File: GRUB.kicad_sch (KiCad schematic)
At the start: 52 parts, among them J1 External controller, timer or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, J3 LEDs Drivers Connector, Q1 2N3904, Q2 2N3904, Q3 2N3904, Q5 2N3904, SW1 R_SWITCH, SW2 U_SWITCH, SW3 B_SWITCH, SW4 1) Focus 2) Safelight 3) Colo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

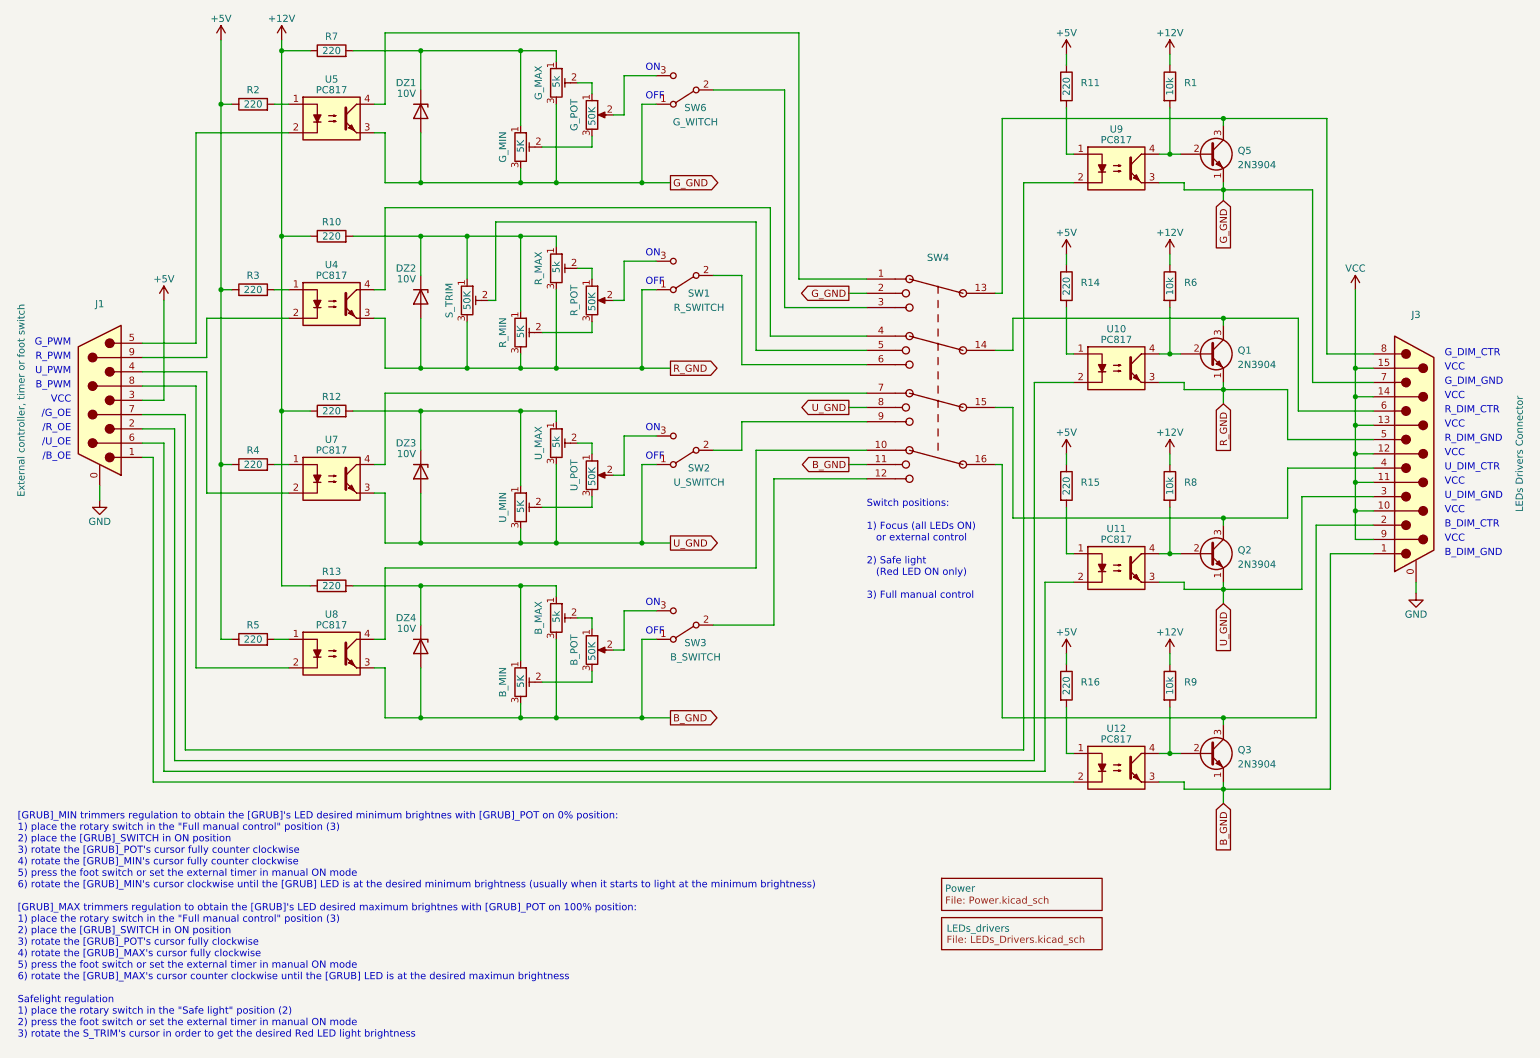
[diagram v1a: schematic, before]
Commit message: - Power rack alternatives: either two LM317s or LM7812 + LM7805 - Added channels SPDT selectors for foot switch or external output enable control
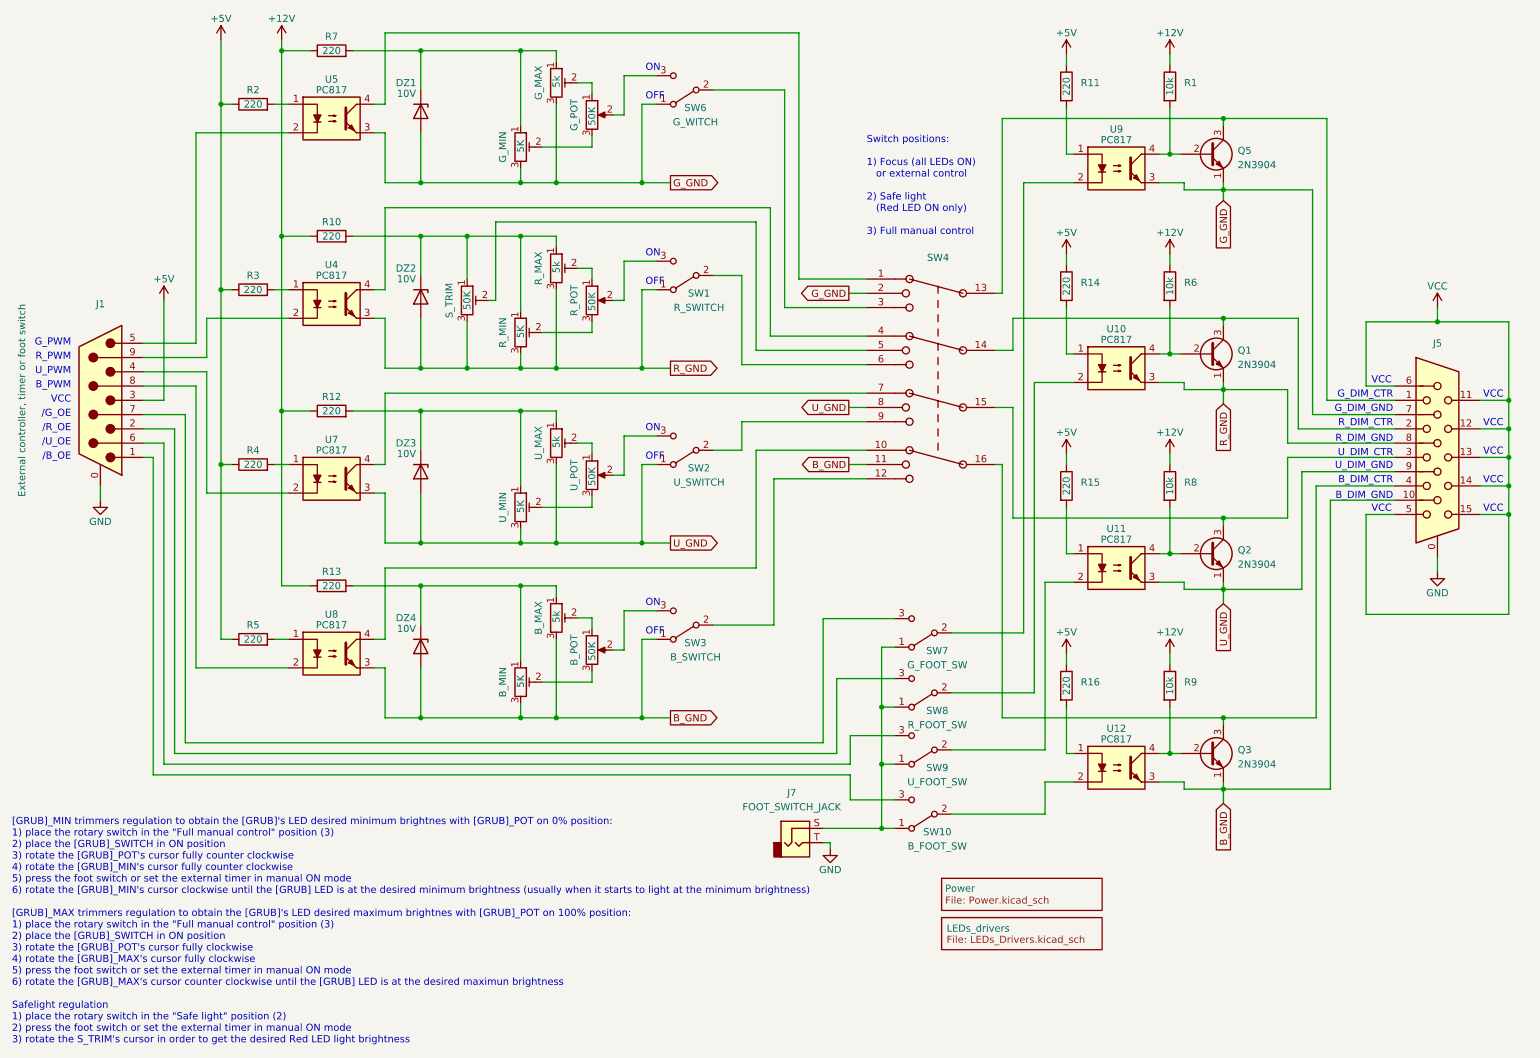
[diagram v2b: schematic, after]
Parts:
- removed J3: LEDs Drivers Connector, symbol Connector:DB15_Male_MountingHoles
- added J5: DE15_Receptacle_HighDensity_MountingHoles, symbol Connector:DE15_Receptacle_HighDensity_MountingHoles
- added J7: FOOT_SWITCH_JACK, symbol Connector_Audio:AudioJack2
- added SW10: B_FOOT_SW, symbol Switch:SW_SPDT
- added SW7: G_FOOT_SW, symbol Switch:SW_SPDT
- added SW8: R_FOOT_SW, symbol Switch:SW_SPDT
- added SW9: U_FOOT_SW, symbol Switch:SW_SPDT
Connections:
- net B_GND: now also J5.10
- net GND: now also J5.0, J7.T
- net G_GND: now also J5.7
- net R_GND: now also J5.8
- net U_GND: now also J5.9
- net VCC: now also J5.11, J5.12, J5.13, J5.14, J5.15, J5.5, J5.6
- net at U11.2: now also SW9.2 (B); no longer J1.6
- net at U12.2: now also SW10.2 (B); no longer J1.1
- net at Q5.3 (C), SW4.13: now also J5.1
- net at Q1.3 (C), SW4.14: now also J5.2
- net at Q2.3 (C), SW4.15: now also J5.3
- net at Q3.3 (C), SW4.16: now also J5.4
- net at U9.2: now also SW7.2 (B); no longer J1.7
- net at U10.2: now also SW8.2 (B); no longer J1.2
- new net: J7.S, SW10.1 (A), SW7.1 (A), SW8.1 (A), SW9.1 (A)
- new net: J1.7, SW7.3 (C)
- new net: J1.2, SW8.3 (C)
- new net: J1.1, SW10.3 (C)
- new net: J1.6, SW9.3 (C)

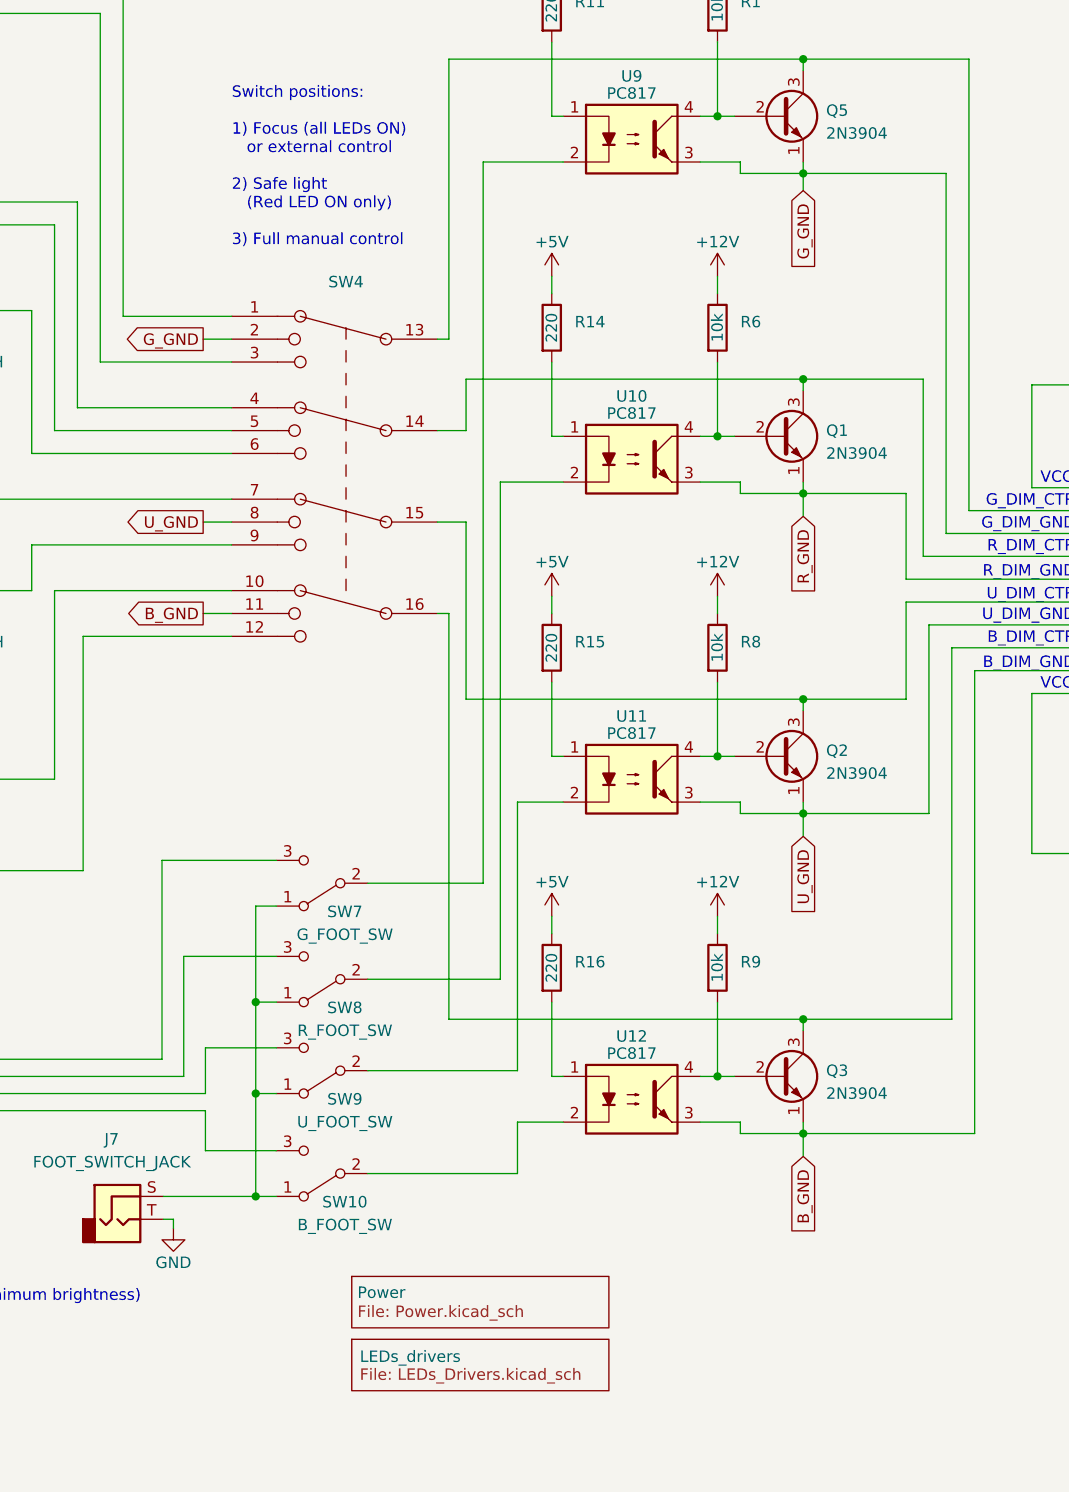
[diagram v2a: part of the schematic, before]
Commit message: Adding metronome commanded by foot switch
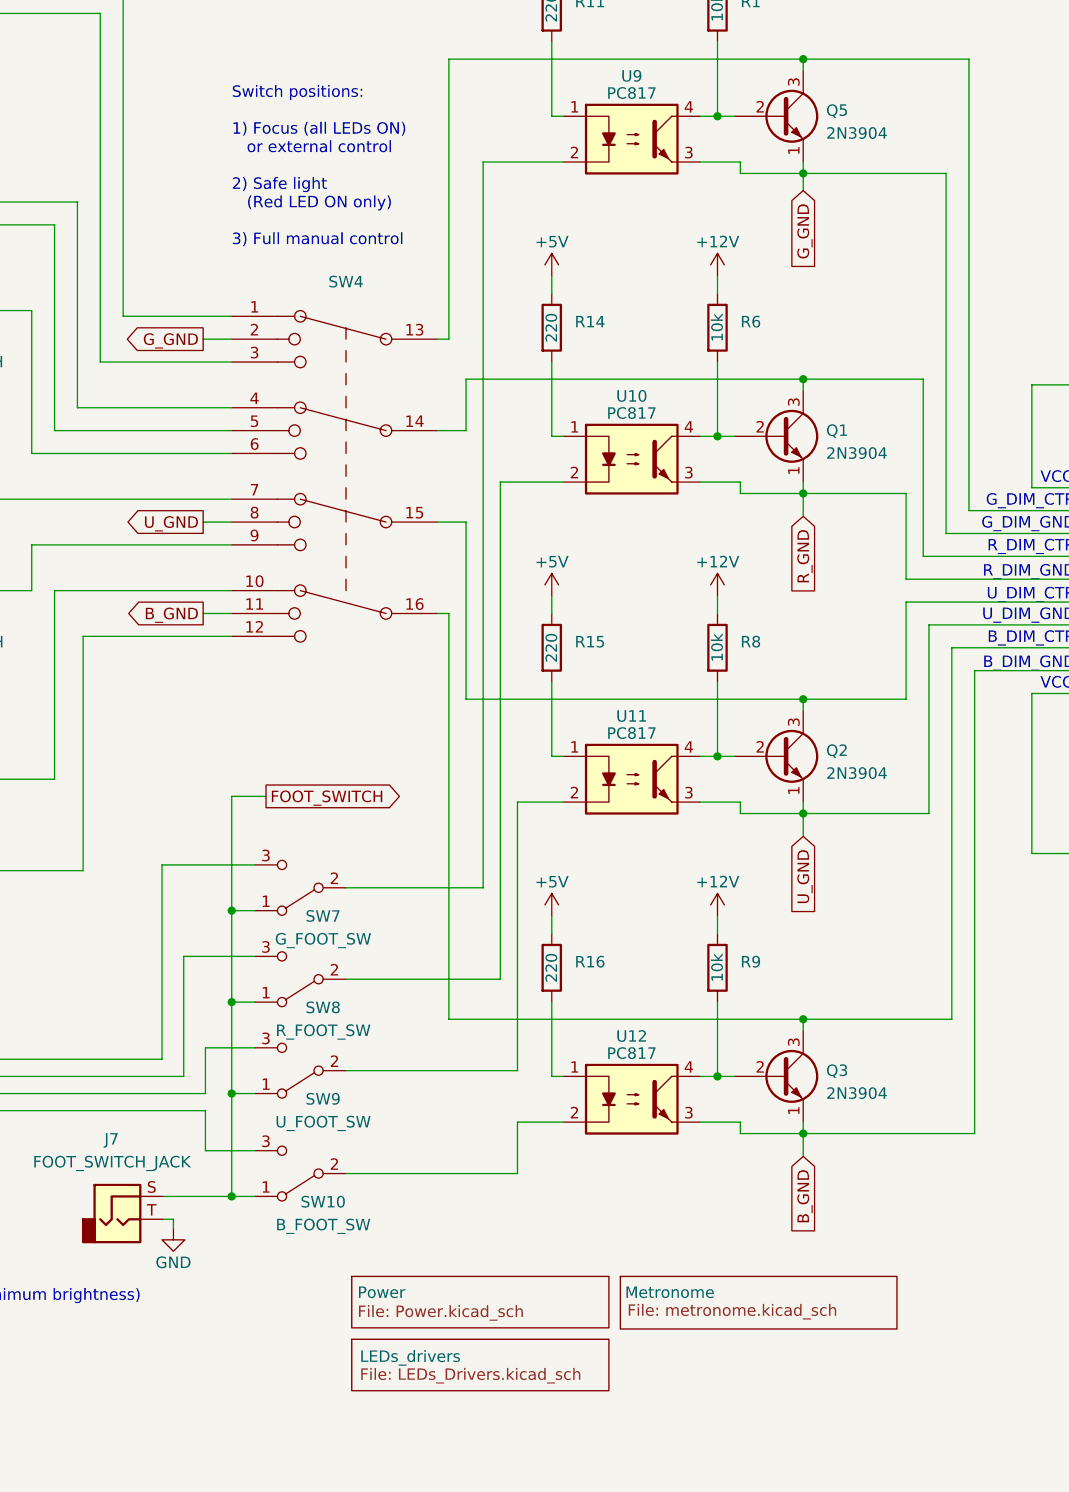
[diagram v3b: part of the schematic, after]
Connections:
- net FOOT_SWITCH: now reaches J7.S, SW10.1 (A), SW7.1 (A), SW8.1 (A), SW9.1 (A)
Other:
- added sheet Metronome (metronome.kicad_sch)
- moved on the sheet: SW10, SW7, SW8, SW9

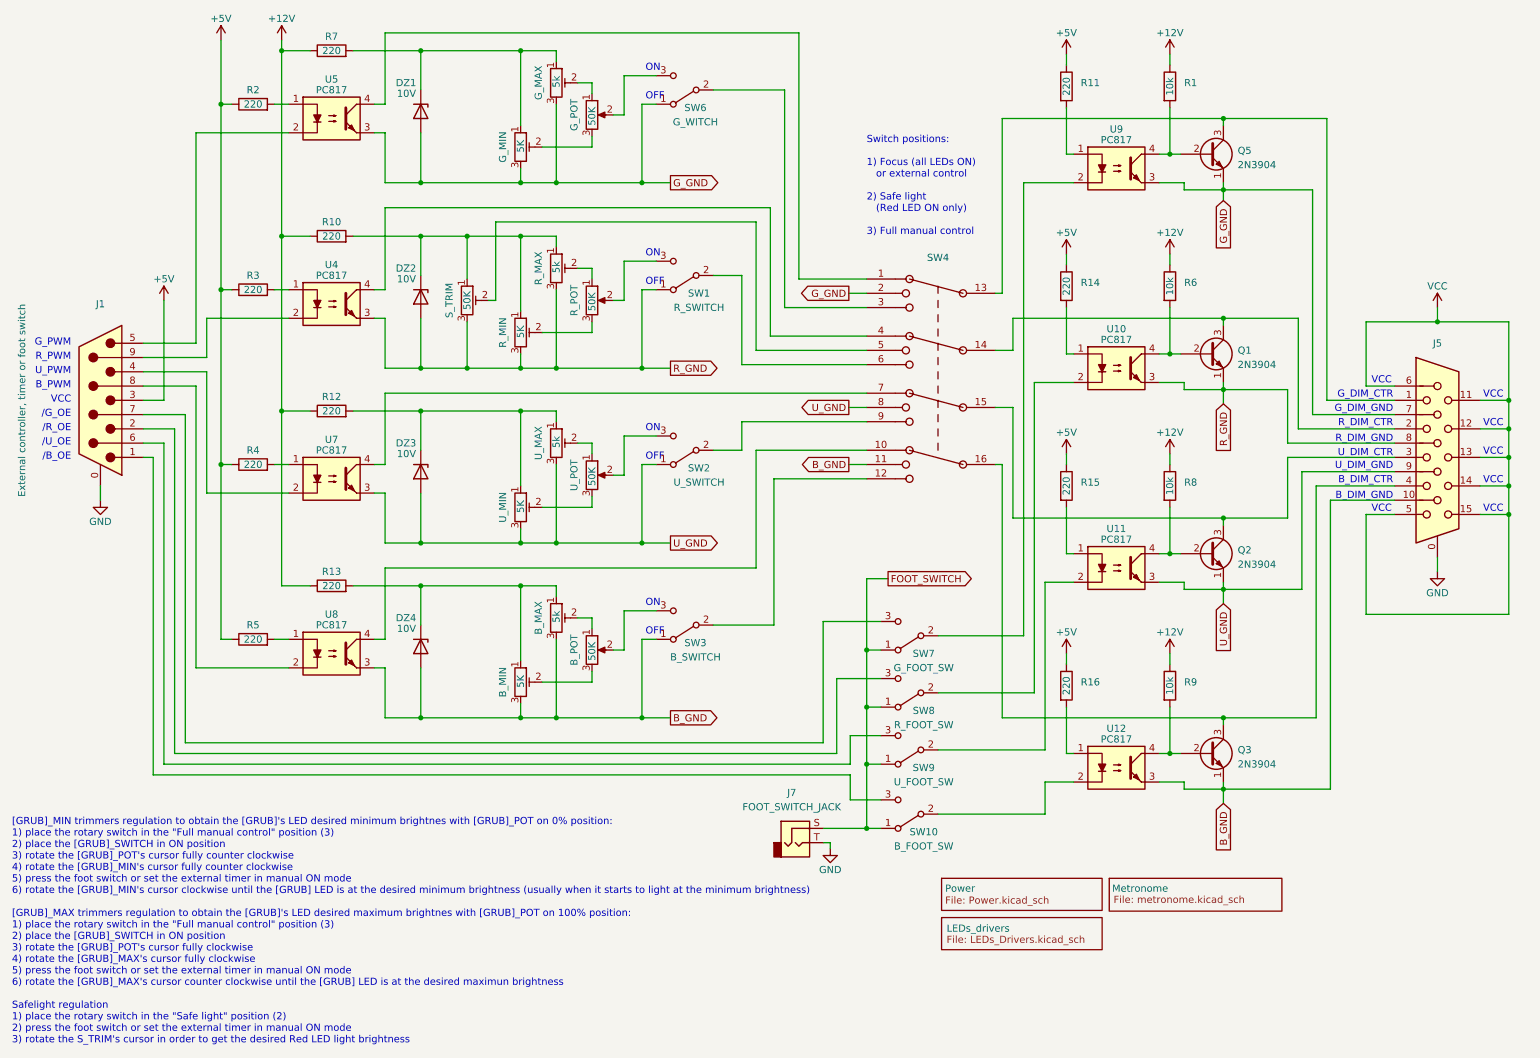
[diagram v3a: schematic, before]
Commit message: Show a couple of R values in metronome circuit depending on speaker resistance
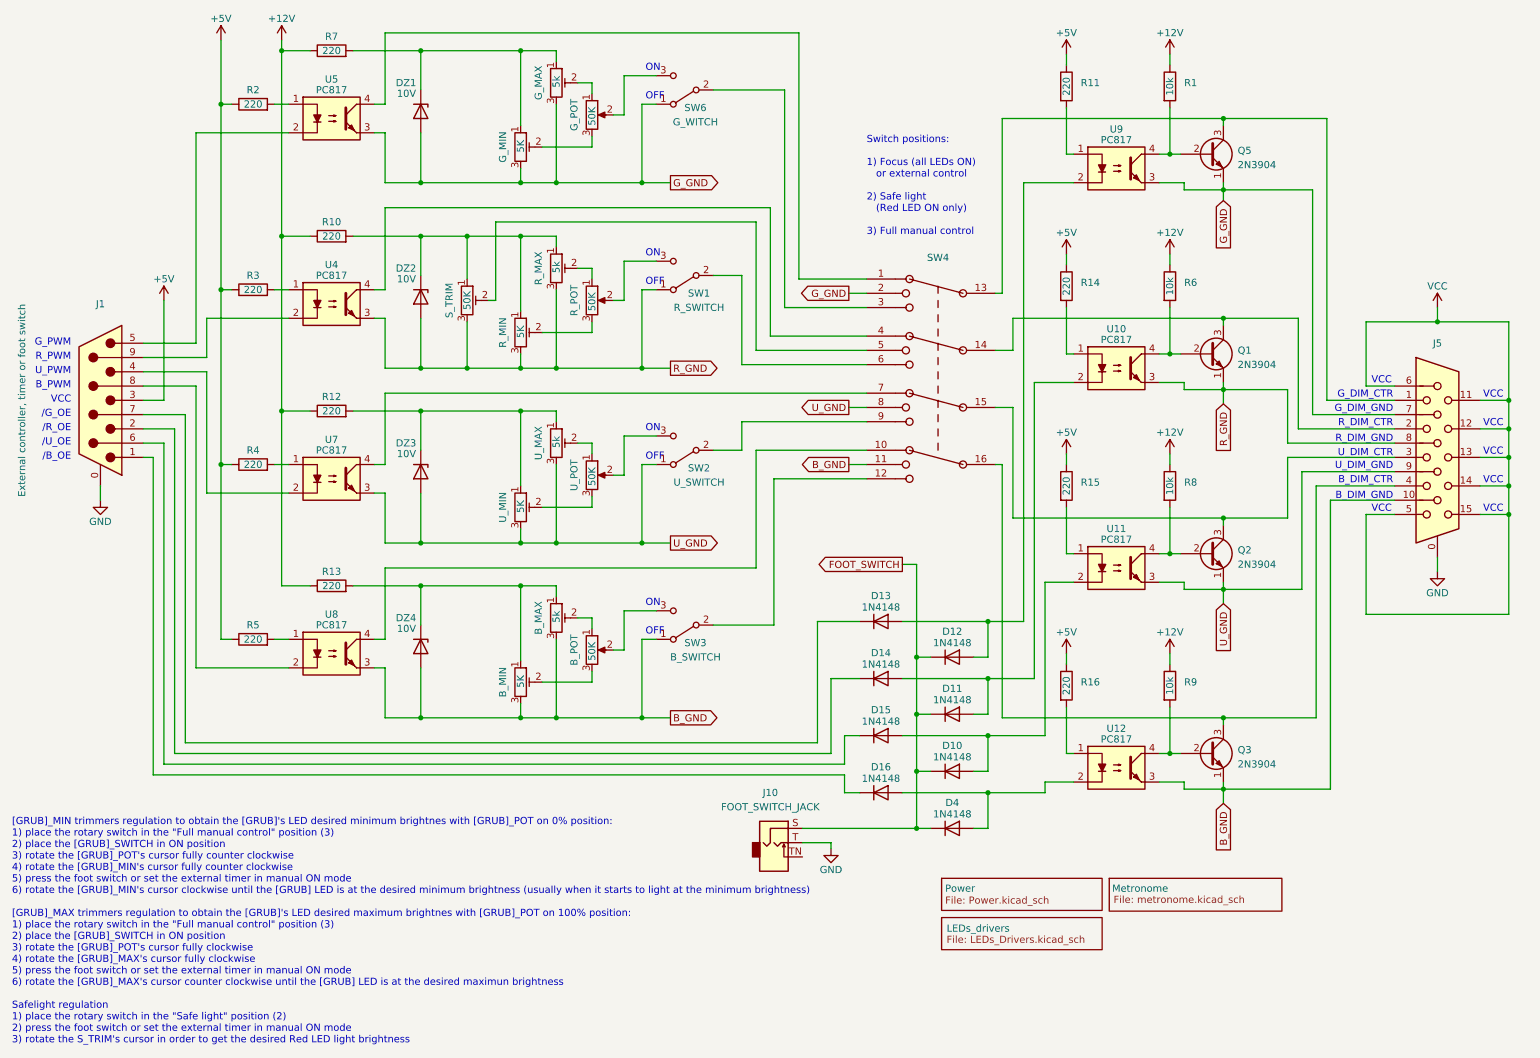
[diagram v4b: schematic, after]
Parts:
- removed J7: FOOT_SWITCH_JACK, symbol Connector_Audio:AudioJack2
- removed SW10: B_FOOT_SW, symbol Switch:SW_SPDT
- removed SW7: G_FOOT_SW, symbol Switch:SW_SPDT
- removed SW8: R_FOOT_SW, symbol Switch:SW_SPDT
- removed SW9: U_FOOT_SW, symbol Switch:SW_SPDT
- added D10, D11, D12, D13, D14, D15, D16, D4: 1N4148, Diode_THT:D_DO-35_SOD27_P7.62mm_Horizontal, symbol Diode:1N4148
- added J10: FOOT_SWITCH_JACK, symbol Connector_Audio:AudioJack2_SwitchT
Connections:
- net FOOT_SWITCH: now also D10.1 (K), D11.1 (K), D12.1 (K), D4.1 (K), J10.S
- net GND: now also J10.T
- net at U11.2: now also D10.2 (A), D15.2 (A)
- net at U9.2: now also D12.2 (A), D13.2 (A)
- net at J1.7: now also D13.1 (K)
- net at U12.2: now also D16.2 (A), D4.2 (A)
- net at U10.2: now also D11.2 (A), D14.2 (A)
- net at J1.2: now also D14.1 (K)
- net at J1.1: now also D16.1 (K)
- net at J1.6: now also D15.1 (K)
